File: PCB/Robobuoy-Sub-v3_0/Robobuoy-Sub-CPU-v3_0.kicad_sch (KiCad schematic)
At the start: 58 parts, among them J201 Prog, J202 ESC_BB, Q201 MMBT3904, Q202 MMBT5401, Q203 MMBT5401, Q204 MMBT3904, Q205 AO3400A, SW201 ~{RESET}, SW202 MODE, U201 LM1117S-3.3, U202 ESP32-WROOM-32E_(visible_peri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, U203 LSM303AGRTR

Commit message: PCB changes
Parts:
- removed C216: 1n, A_Device:C_0603, symbol Device:C_Small
- added H202, H203, H204: MountingHole, MountingHole:MountingHole_3.2mm_M3, symbol Mechanical:MountingHole
- added J202: I2C, Connector_JST:JST_XH_B4B-XH-A_1x04_P2.50mm_Vertical, symbol Connector:Conn_01x04_Socket
- added R208: 10K, A_Device:R_0603, symbol Device:R
- renumbered C217 to C216, C218 to C217, C219 to C218, C220 to C219, C221 to C220, C222 to C221, C223 to C222, C224 to C223, C225 to C224, J202 to J203, R208 to R209, R209 to R210, R210 to R211, R211 to R212, R212 to R213, R213 to R214
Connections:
- net +3.3V: now also R208.2
- net +5V: now also J202.3 (Pin_3)
- net GND: now also J202.4 (Pin_4)
- net RX_SUB: now also R208.1
- net SCL: now reaches R212.2, U202.36 (SCL/GPIO22), U203.1 (SCL/SPC)
- net SCL: now also J202.1 (Pin_1)
- net SDA: now reaches R211.2, U202.33 (SDA/GPIO21), U203.4 (SDA/SDI/SDO)
- net SDA: now also J202.2 (Pin_2)
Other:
- moved on the sheet: H201

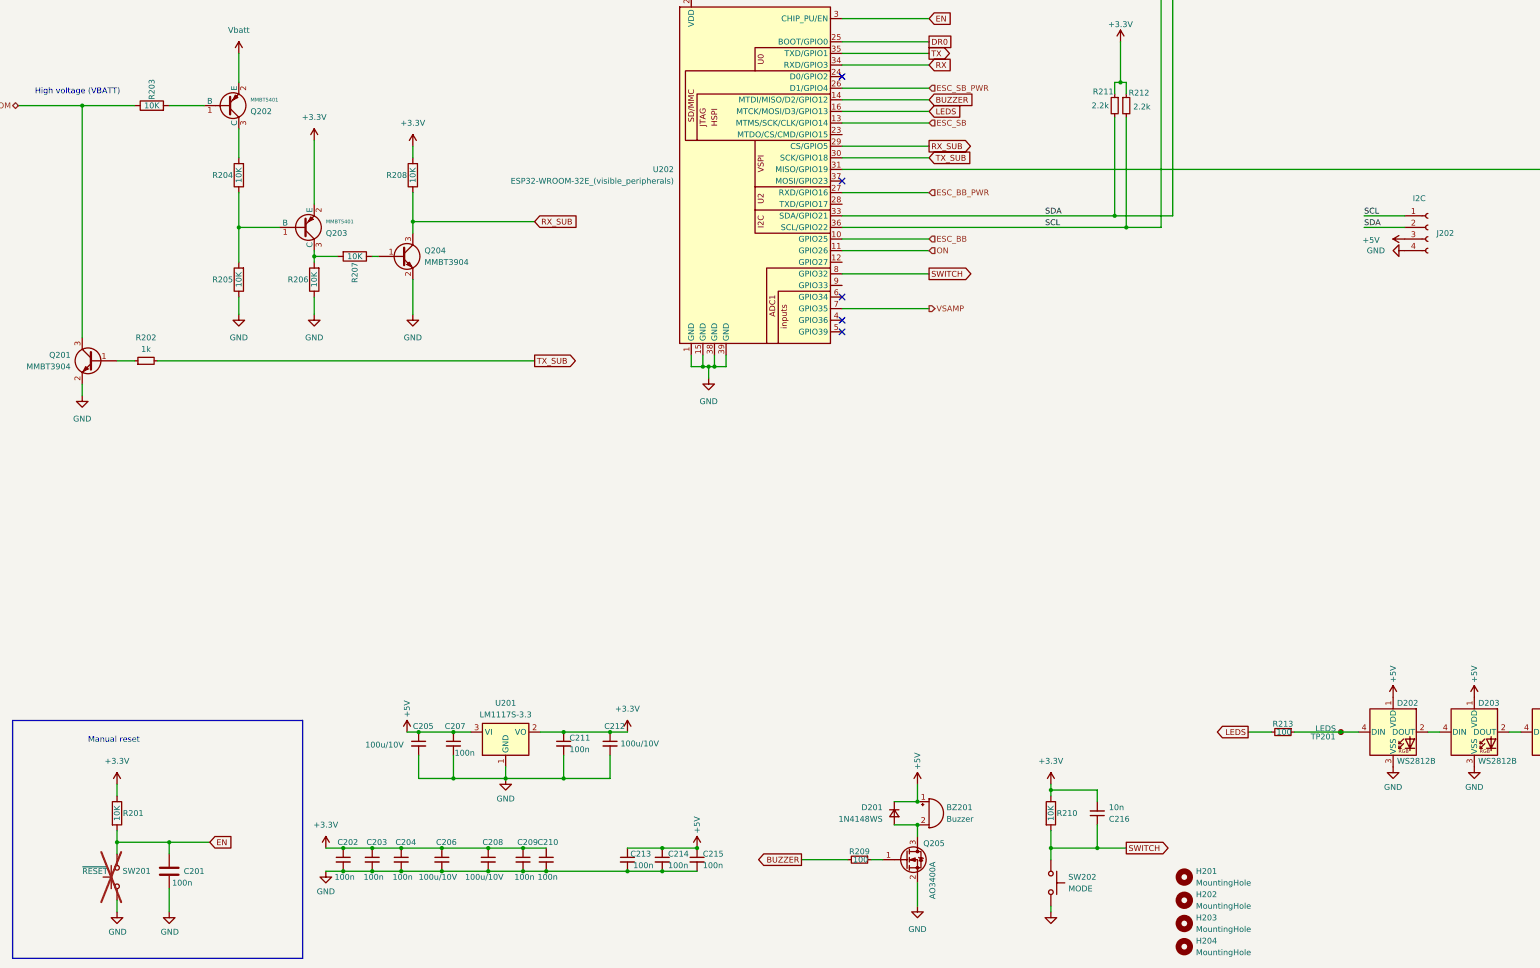
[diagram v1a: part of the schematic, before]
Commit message: PCB 3.0 almoste finished Imon calculation added
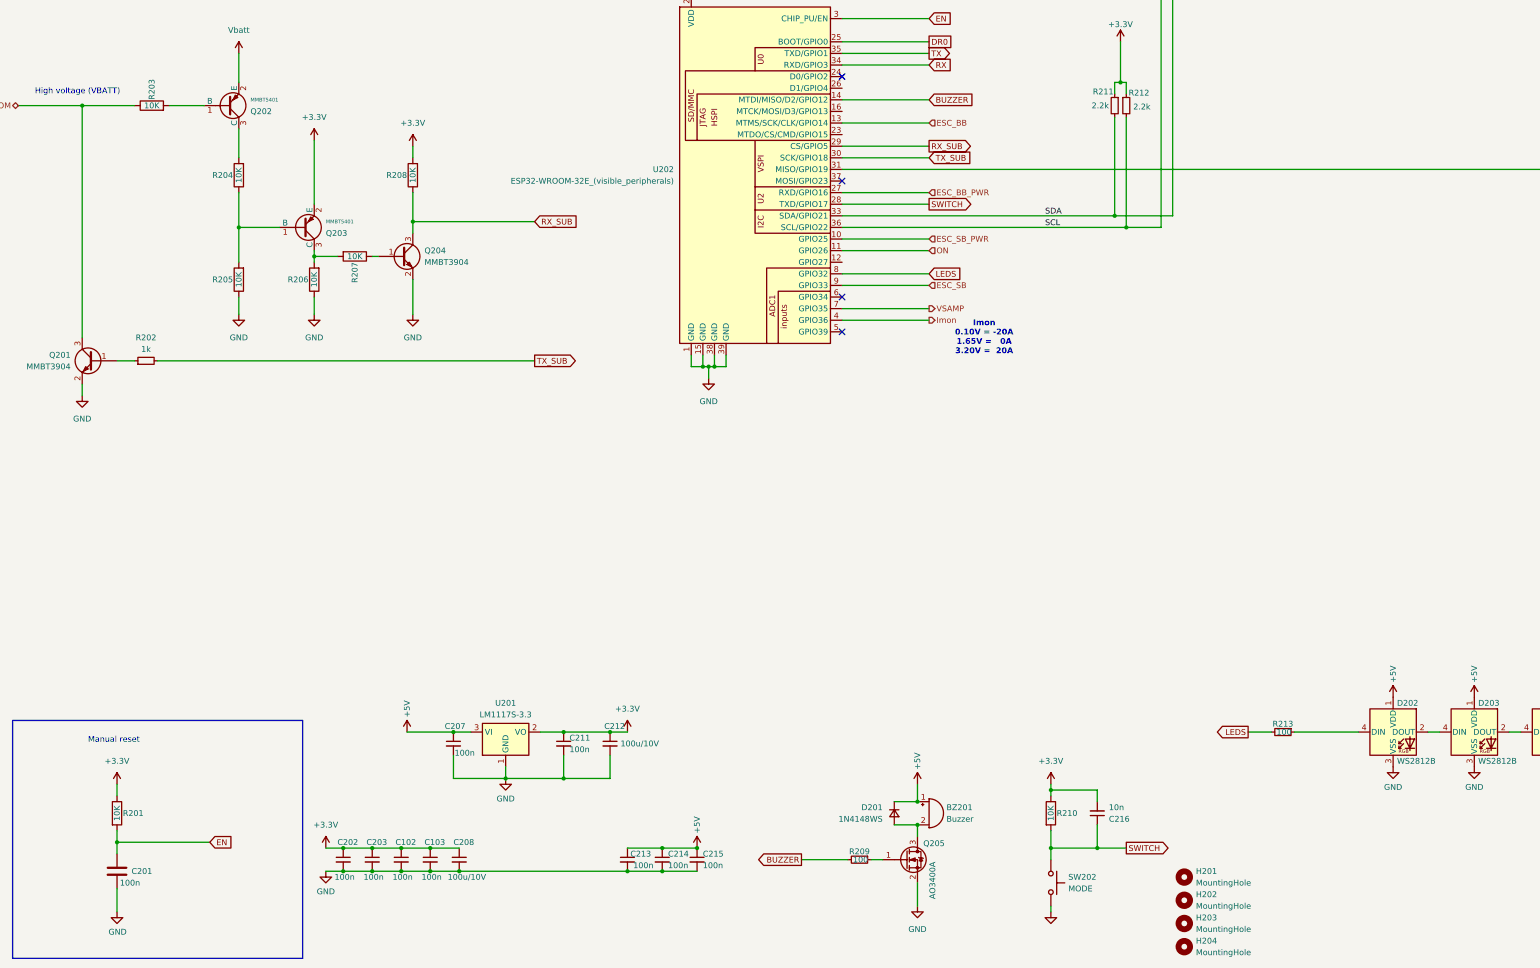
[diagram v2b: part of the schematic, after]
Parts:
- removed C204, C209, C210: 100n, A_Device:C_0603, symbol Device:C_Small
- removed C205, C206: 100u/10V, Capacitor_SMD:C_1210_3225Metric, symbol Device:C_Small
- removed J202: I2C, Connector_JST:JST_XH_B4B-XH-A_1x04_P2.50mm_Vertical, symbol Connector:Conn_01x04_Socket
- removed SW201: ~{RESET}, Connector_PinHeader_2.54mm:PinHeader_1x02_P2.54mm_Vertical, symbol Switch:SW_Push
- removed TP201: LEDS, A_Pads_Pins:Testpad_1, symbol Connector:TestPoint_Small
- added C102, C103: 100n, A_Device:C_0603, symbol Device:C_Small
- BZ201: footprint A_Misc:Buzzer-12x6.5x5.2 -> A_Connector:Header_1x02_P2.54_Jumper
- J203: footprint Connector_JST:JST_XH_B3B-XH-A_1x03_P2.50mm_Vertical -> A_Connector:Header_1x03_P2.54_Male
- SW202: footprint Button_Switch_SMD:SW_SPST_TL3342 -> A_Connector:Header_1x02_P2.54_Jumper; LCSC C318884 -> (none)
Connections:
- net +3.3V: now also C102.1, C103.1
- net ESC_BB: now also U202.13 (MTMS/SCK/CLK/GPIO14); no longer U202.10 (GPIO25)
- net ESC_SB: now also U202.9 (GPIO33); no longer U202.13 (MTMS/SCK/CLK/GPIO14)
- net ESC_SB_PWR: now also U202.10 (GPIO25); no longer U202.26 (D1/GPIO4)
- net GND: now also C102.2, C103.2
- net LEDS: now also U202.8 (GPIO32); no longer U202.16 (MTCK/MOSI/D3/GPIO13)
- net SWITCH: now also U202.28 (TXD/GPIO17); no longer U202.8 (GPIO32)
- net Imon: now reaches U202.4 (GPIO36)
- no-connect marks 7 -> 6
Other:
- note added: "Imon 0.10V = -20A 1.65V = 0A 3.20V = 20A"
- moved on the sheet: C201, C208

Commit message: pcb ready for production
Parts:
- removed C217, C223: 1n, A_Device:C_0603, symbol Device:C_Small
- removed C218, C220: 10n, A_Device:C_0603, symbol Device:C_Small
- removed C219, C221, C224: 100n, A_Device:C_0603, symbol Device:C_Small
- removed C222: 100u/10V, Capacitor_SMD:C_1210_3225Metric, symbol Device:C_Small
- removed FB201: 0.3E 240E@100MHz, A_Device:L_0805_(1.2), symbol Device:FerriteBead_Small
- removed U203: LSM303AGRTR, A_Device:LGA-12_2x2mm_P0.5mm, symbol Sensor_Motion:LSM303C
- added J102: Display, A_Connector:Header_1x04_P2.54_Male, symbol Connector:Conn_01x04_Socket
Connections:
- net +3.3V: now also J102.2 (Pin_2)
- net GND: now also J102.1 (Pin_1)
- net SCL: now also J102.3 (Pin_3)
- net SDA: now also J102.4 (Pin_4)
- no-connect marks 6 -> 4
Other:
- added sheet Compass (untitled.kicad_sch)
- note removed: "Compass"
- moved on the sheet: R211, R212

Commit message: Last cosmetic cleanupt
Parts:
- removed H201, H202, H203, H204: MountingHole, MountingHole:MountingHole_3.2mm_M3, symbol Mechanical:MountingHole
- BZ201, J201, J203, SW202: now not fitted

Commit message: Simulation added bms Little improvements BMS Resistor divider added on the gate of the mosfet (Limmeded to +/-20V could be 30V during charging)
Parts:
- removed Q201, Q204: MMBT3904, Package_TO_SOT_SMD:SOT-23, symbol Transistor_BJT:BC847
- removed Q202, Q203: MMBT5401, PCM_JLCPCB:Q_SOT-23, symbol PCM_JLCPCB-Transistors:PNP,MMBT5401
- removed R202: 1k, A_Device:R_0603, symbol Device:R_Small
- removed R203, R204, R205, R206, R207, R208: 10K, A_Device:R_0603, symbol Device:R
- added D205: GREEN, LED_SMD:LED_0603_1608Metric, symbol Device:LED_Small
- added R212: 2.2k, A_Device:R_0603, symbol Device:R_Small
- BZ201, J201, J203, SW202: now left out of the parts list
- J102: value Display -> I2C_OUT
- R201, R210: value 10K -> 10k
- renumbered R212 to R104
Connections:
- net +3.3V: now also R212.1
- net ESC_BB: now also U202.9 (GPIO33); no longer U202.13 (MTMS/SCK/CLK/GPIO14)
- net ESC_BB_PWR: now also U202.10 (GPIO25); no longer U202.27 (RXD/GPIO16)
- net ESC_SB: now also U202.13 (MTMS/SCK/CLK/GPIO14); no longer U202.9 (GPIO33)
- net ESC_SB_PWR: now also U202.27 (RXD/GPIO16); no longer U202.10 (GPIO25)
- net GND: now also D205.1 (K)
- net SCL: now also R212.2; no longer R104.2
- new net: D205.2 (A), R104.2
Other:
- note added: "LEDS"
- note added: "Powersupply"
- note added: "Reset"
- note removed: "High voltage (VBATT)"
- note removed: "Manual reset"
- moved on the sheet: BZ201, C102, C103, C201, C202, C203, C207, C208, C211, C212, C213, C214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

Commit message: PCB adjustmend Sub V3.0
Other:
- sheet Compass: file untitled.kicad_sch -> Robobuoy-Sub_Compass-v3_0.kicad_sch
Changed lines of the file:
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@@
 	)
 	(sheet
-		(at 295.402 130.81)
-		(size 38.354 30.48)
+		(at 296.164 130.81)
+		(size 37.592 35.814)
 		(exclude_from_sim no)
 		(in_bom yes)
@@
 		)
 		(property "Sheetname" "Compass"
-			(at 295.402 130.0984 0)
+			(at 296.164 130.0984 0)
 			(effects
 				(font
@@
 			)
 		)
-		(property "Sheetfile" "untitled.kicad_sch"
-			(at 295.402 161.8746 0)
+		(property "Sheetfile" "Robobuoy-Sub_Compass-v3_0.kicad_sch"
+			(at 296.164 167.2086 0)
 			(effects
 				(font
@@
 			(project "Robobuoy-Sub-v3_0"
 				(path "/b4d50f7c-16b2-4c5a-bb6a-7ca43079286e/e351be3e-b038-437a-bd8d-55f566134198"
-					(page "4")
+					(page "5")
 				)
 			)

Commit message: BMS asd SUB orderd at JLCPCB
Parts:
- D205: LCSC C2286 -> C12624
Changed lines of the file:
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@@
 			)
 		)
-		(property "LCSC" "C2286"
+		(property "LCSC" "C12624"
 			(at 71.12 259.08 0)
 			(effects
